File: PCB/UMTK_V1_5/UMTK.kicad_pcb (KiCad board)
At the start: 4 copper layers, 170 x 80 mm, 97 parts, among them J1 Motor Out, J2 ESTOP, J3 LOADCELL, J5 PJ-102BH, J8 10033526-N3212LF, Q1 Q_PNP_BEC, U1 DRV8873SPWPRQ1, U10 LM2576HVS-5, U11 SN74LVC1T45DCK, U12 SN74LVC1T45DCK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

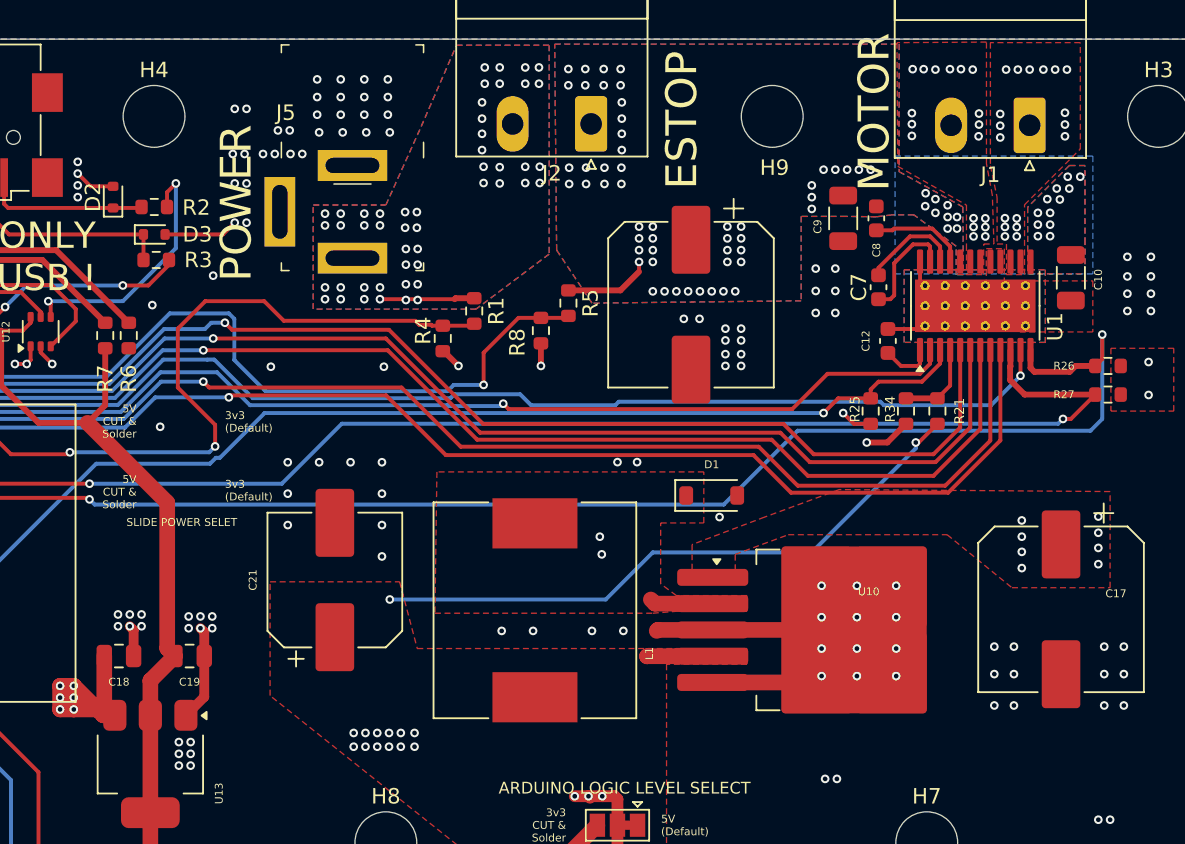
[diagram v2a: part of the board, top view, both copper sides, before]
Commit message: Add a bit of decoupling for 7seg driver
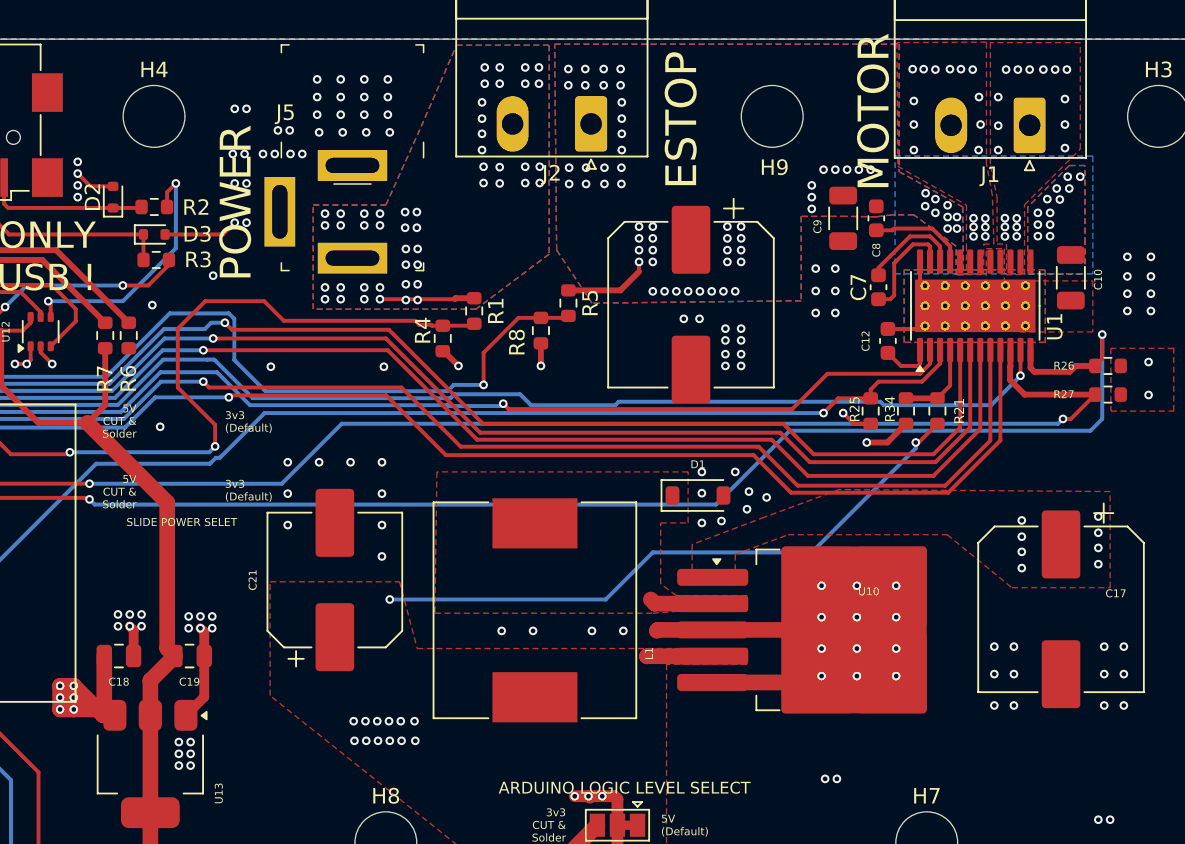
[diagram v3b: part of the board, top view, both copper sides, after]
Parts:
- moved D1 0.89 mm to (155.2, 49.5)
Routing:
- net GND: vias 269 -> 272
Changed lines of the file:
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@@
 	(footprint "Diode_SMD:D_SOD-123"
 		(layer "F.Cu")
-		(at 156.083 49.53)
+		(at 155.195 49.53)
 		(descr "SOD-123")
 		(tags "SOD-123")
@@
 	)
 	(via
+		(at 158.369 50.419)
+		(size 0.56)
+		(drill 0.3)
+		(layers "F.Cu" "B.Cu")
+		(free yes)
+		(net 4)
+	)
+	(via
 		(at 30.226 59.69)
 		(size 0.56)
@@
 	)
 	(via
-		(at 148.971 53.34)
-		(size 0.56)
-		(drill 0.3)
-		(layers "F.Cu" "B.Cu")
-		(free yes)
-		(net 4)
-	)
-	(via
 		(at 46.99 36.703)
 		(size 0.56)
@@
 	)
 	(via
+		(at 155.448 49.382)
+		(size 0.56)
+		(drill 0.3)
+		(layers "F.Cu" "B.Cu")
+		(free yes)
+		(net 4)
+	)
+	(via
 		(at 121.605 67.009)
 		(size 0.56)
@@
 	)
 	(via
-		(at 149.987 47.371)
+		(at 155.448 51.308)
+		(size 0.56)
+		(drill 0.3)
+		(layers "F.Cu" "B.Cu")
+		(free yes)
+		(net 4)
+	)
+	(via
+		(at 157.607 48.006)
 		(size 0.56)
 		(drill 0.3)
@@
 	)
 	(via
-		(at 156.591 50.927)
+		(at 156.718 51.181)
 		(size 0.56)
 		(drill 0.3)
@@
 	)
 	(via
+		(at 158.496 49.276)
+		(size 0.56)
+		(drill 0.3)
+		(layers "F.Cu" "B.Cu")
+		(free yes)
+		(net 4)
+	)
+	(via
 		(at 157.988 38.735)
 		(size 0.56)
@@
 	)
 	(via
-		(at 148.844 52.196998)
+		(at 115.062 29.464)
 		(size 0.56)
 		(drill 0.3)
@@
 	)
 	(via
-		(at 115.062 29.464)
+		(at 122.24 57.357)
 		(size 0.56)
 		(drill 0.3)
 		(layers "F.Cu" "B.Cu")
-		(free yes)
 		(net 4)
 	)
 	(via
-		(at 122.24 57.357)
+		(at 159.639 49.657)
 		(size 0.56)
 		(drill 0.3)
 		(layers "F.Cu" "B.Cu")
+		(free yes)
 		(net 4)
 	)
@@
 	)
 	(via
-		(at 151.257 47.371)
+		(at 155.448 48.006)
 		(size 0.56)
 		(drill 0.3)
@@
 	)
 	(via
-		(at 133.6802 64.897)
+		(at 133.6802 64.135)
 		(size 0.56)
 		(drill 0.3)
@@
 	)
 	(via
-		(at 134.4422 65.786)
+		(at 134.493 65.405)
 		(size 0.56)
 		(drill 0.3)
@@
 	)
 	(via
-		(at 135.9662 65.786)
+		(at 136.017 65.405)
 		(size 0.56)
 		(drill 0.3)
@@
 	)
 	(via
-		(at 134.4422 64.897)
+		(at 134.4422 64.135)
 		(size 0.56)
 		(drill 0.3)
@@
 	)
 	(via
-		(at 132.9182 64.897)
+		(at 132.9182 64.135)
 		(size 0.56)
 		(drill 0.3)
@@
 	)
 	(via
-		(at 132.9182 65.786)
+		(at 132.969 65.405)
 		(size 0.56)
 		(drill 0.3)
@@
 	)
 	(via
-		(at 135.2042 64.897)
+		(at 135.2042 64.135)
 		(size 0.56)
 		(drill 0.3)
@@
 	)
 	(via
-		(at 136.8552 64.897)
+		(at 136.8552 64.135)
 		(size 0.56)
 		(drill 0.3)
@@
 	)
 	(via
-		(at 135.2042 65.786)
+		(at 135.255 65.405)
 		(size 0.56)
 		(drill 0.3)
@@
 	)
 	(via
-		(at 133.6802 65.786)
+		(at 133.731 65.405)
 		(size 0.56)
 		(drill 0.3)
@@
 	)
 	(via
-		(at 136.8552 65.786)
+		(at 136.906 65.405)
 		(size 0.56)
 		(drill 0.3)
@@
 	)
 	(via
-		(at 135.9662 64.897)
+		(at 135.9662 64.135)
 		(size 0.56)
 		(drill 0.3)
@@
 	)
 	(segment
-		(start 161.644724 45.339)
-		(end 180.594 45.339)
+		(start 180.594 45.339)
+		(end 181.356 44.577)
 		(width 0.254)
 		(layer "B.Cu")
@@
 	)
 	(segment
-		(start 116.159 50.119)
-		(end 156.864724 50.119)
+		(start 156.356724 50.119)
+		(end 161.136724 45.339)
 		(width 0.254)
 		(layer "B.Cu")
@@
 	)
 	(segment
-		(start 115.824 49.784)
-		(end 116.159 50.119)
+		(start 161.136724 45.339)
+		(end 180.594 45.339)
 		(width 0.254)
 		(layer "B.Cu")
@@
 	)
 	(segment
-		(start 180.594 45.339)
-		(end 181.356 44.577)
+		(start 116.159 50.119)
+		(end 156.356724 50.119)
 		(width 0.254)
 		(layer "B.Cu")
@@
 	)
 	(segment
-		(start 156.864724 50.119)
-		(end 161.644724 45.339)
+		(start 115.824 49.784)
+		(end 116.159 50.119)
 		(width 0.254)
 		(layer "B.Cu")
@@
 	)
 	(via
-		(at 169.037 24.7904)
+		(at 169.164 24.003)
 		(size 0.56)
 		(drill 0.3)
@@
 	)
 	(via
-		(at 169.037 25.5016)
+		(at 169.164 25.527)
 		(size 0.56)
 		(drill 0.3)
@@
 	)
 	(via
-		(at 173.3804 25.527)
+		(at 173.482 25.527)
 		(size 0.56)
 		(drill 0.3)
@@
 	)
 	(via
-		(at 173.355 26.289)
+		(at 173.355 27.178)
 		(size 0.56)
 		(drill 0.3)
@@
 	)
 	(via
-		(at 173.3804 24.8158)
+		(at 173.3804 23.749)
 		(size 0.56)
 		(drill 0.3)
@@
 	)
 	(via
-		(at 169.037 26.2636)
+		(at 169.164 27.178)
 		(size 0.56)
 		(drill 0.3)
@@
 	)
 	(via
-		(at 174.752 26.3652)
+		(at 174.625 27.178)
 		(size 0.56)
 		(drill 0.3)
@@
 	)
 	(via
-		(at 178.943 24.765)
+		(at 178.943 23.876)
 		(size 0.56)
 		(drill 0.3)
@@
 	)
 	(via
-		(at 178.943 26.289)
+		(at 178.943 27.051)
 		(size 0.56)
 		(drill 0.3)
@@
 	)
 	(via
-		(at 174.752 24.8412)
+		(at 174.625 23.749)
 		(size 0.56)
 		(drill 0.3)
@@
 	)
 	(via
-		(at 174.752 25.6032)
+		(at 174.625 25.6032)
 		(size 0.56)
 		(drill 0.3)
@@
 			(pts
 				(xy 138.303 48.006) (xy 138.176 57.15) (xy 152.273 57.15) (xy 153.797 57.023) (xy 158.369 57.023)
-				(xy 158.369 56.007) (xy 153.797 56.007) (xy 152.781 55.245) (xy 152.781 51.308) (xy 155.575 51.308)
-				(xy 155.575 48.006)
+				(xy 158.369 56.007) (xy 153.797 56.007) (xy 152.781 55.245) (xy 152.781 51.308) (xy 154.559 51.308)
+				(xy 154.559 48.006)
 			)
 		)
@@
 		(hatch edge 0.5)
 		(priority 9)
-		(connect_pads yes
+		(connect_pads thru_hole_only
 			(clearance 0.1524)
 		)
@@
 		(fill yes
 			(thermal_gap 0.5)
-			(thermal_bridge_width 0.5)
+			(thermal_bridge_width 1.016)
 		)
 		(polygon
@@
 		(hatch edge 0.5)
 		(priority 3)
-		(connect_pads yes
+		(connect_pads thru_hole_only
 			(clearance 0.1524)
 		)
@@
 		(fill yes
 			(thermal_gap 0.5)
-			(thermal_bridge_width 0.5)
+			(thermal_bridge_width 1.016)
 		)
 		(polygon
@@
 		(filled_areas_thickness no)
 		(fill yes
-			(thermal_gap 0.5)
-			(thermal_bridge_width 0.5)
+			(thermal_gap 0.508)
+			(thermal_bridge_width 1.016)
 			(island_removal_mode 1)
-			(island_area_min 9.999999)
+			(island_area_min 9.999998)
 		)
 		(polygon
@@
 		(fill yes
 			(thermal_gap 0.5)
-			(thermal_bridge_width 0.5)
+			(thermal_bridge_width 1.016)
 			(island_removal_mode 1)
-			(island_area_min 9.999999)
+			(island_area_min 9.999998)
 		)
 		(polygon

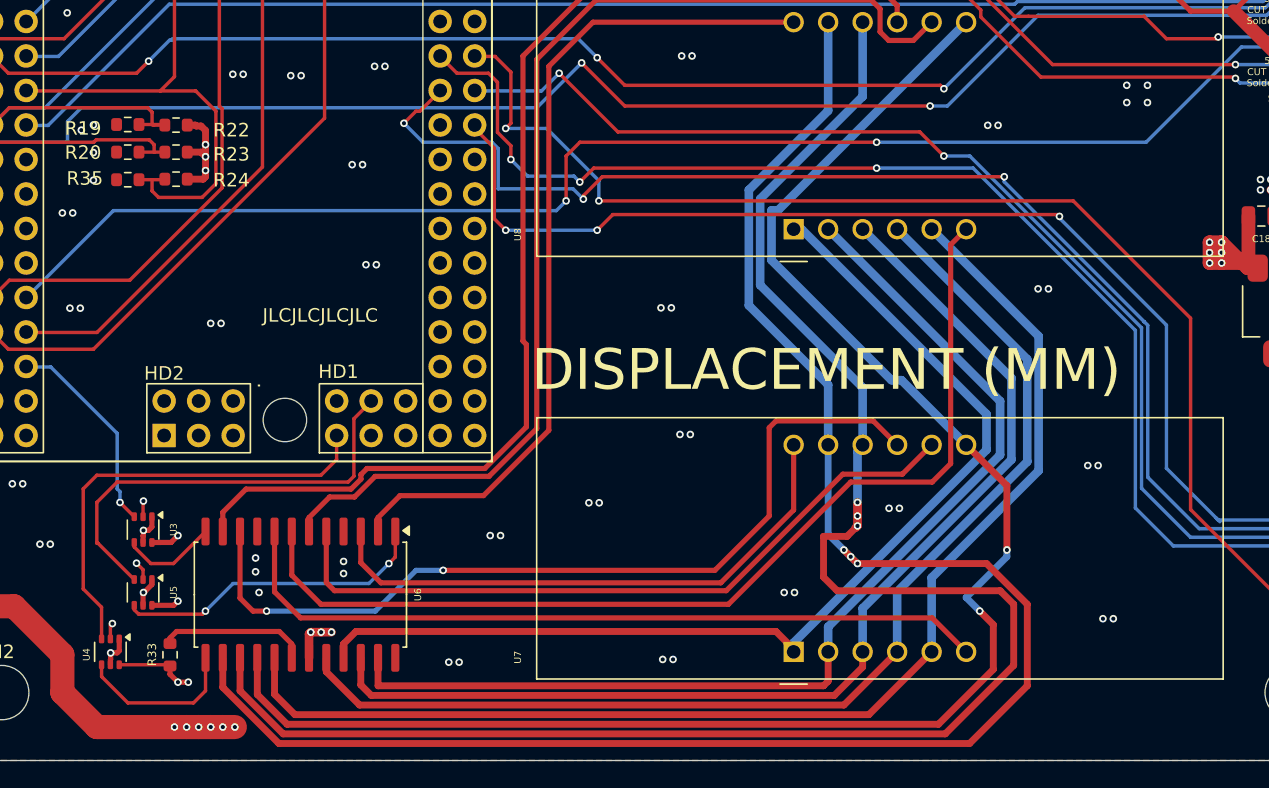
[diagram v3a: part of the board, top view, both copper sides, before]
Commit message: Add devoupling for 7seg
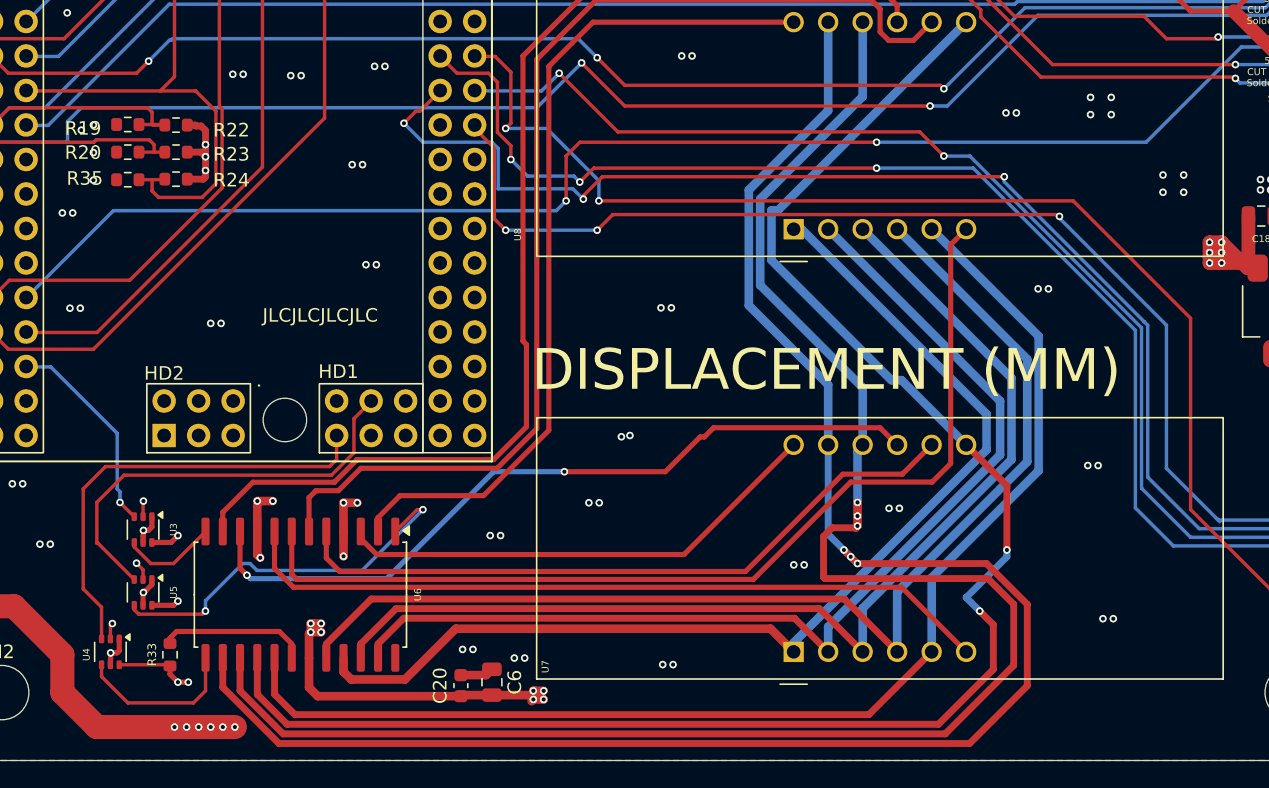
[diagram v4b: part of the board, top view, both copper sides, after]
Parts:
- added C20: 0.1u, Capacitor_SMD:C_0603_1608Metric, F.Cu at (58.8, 94.5)
- added C6: 10u, Capacitor_SMD:C_0805_2012Metric, F.Cu at (61.1, 94.2)
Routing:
- net +5V: track 262.1 -> 287.0 mm, vias 50 -> 55
- net GND: track 65.4 -> 78.2 mm, vias 272 -> 279
- net Net-(U6-DIG_5): track 64.0 -> 56.5 mm
- net Net-(U6-DIG_4): track 41.8 -> 36.2 mm
- net Net-(U5-B): track 23.3 -> 28.5 mm
- net Net-(U6-DIG_6): track 53.0 -> 50.8 mm
- net Net-(U6-SEG_E): track 78.3 -> 79.9 mm
- net Net-(U6-DIG_3): track 74.6 -> 73.1 mm
- net Net-(U6-SEG_D): track 79.1 -> 77.6 mm
- net Net-(U6-DIG_7): track 57.2 -> 56.2 mm
- net /7Seg_Display/DIN: track 32.6 -> 31.6 mm
- net Net-(U6-SEG_DP): track 81.4 -> 80.6 mm
- net Net-(U6-DIG_2): track 81.4 -> 82.2 mm

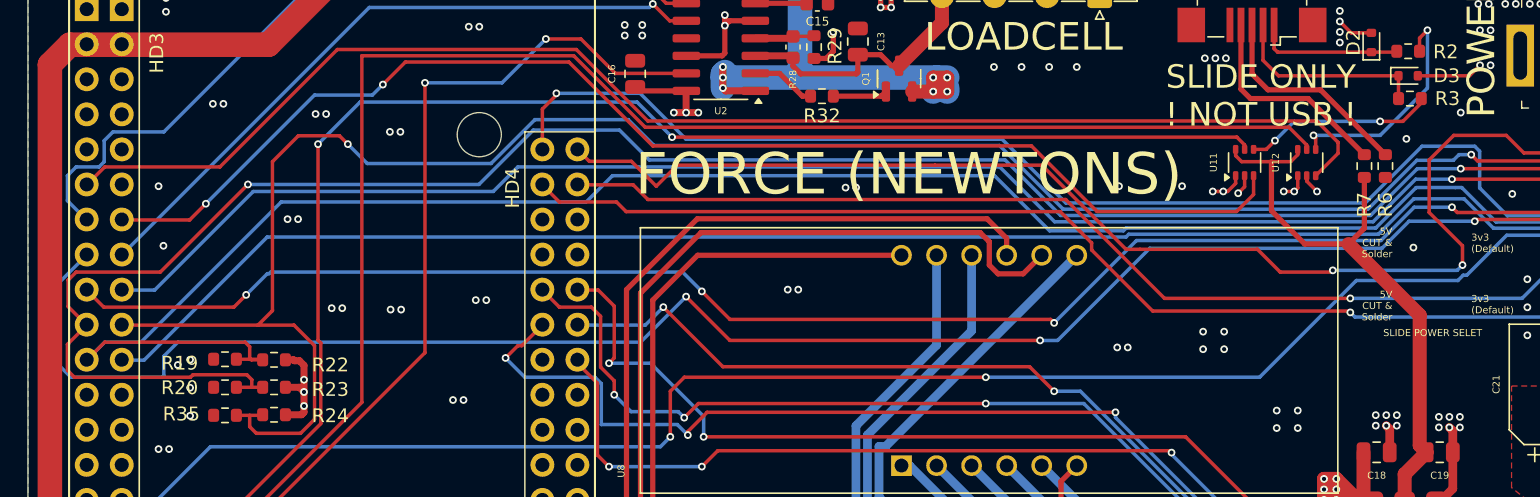
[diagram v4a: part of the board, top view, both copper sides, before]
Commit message: Move interrupr pin to 3, Move motor sleep to 14 so 13 can LED
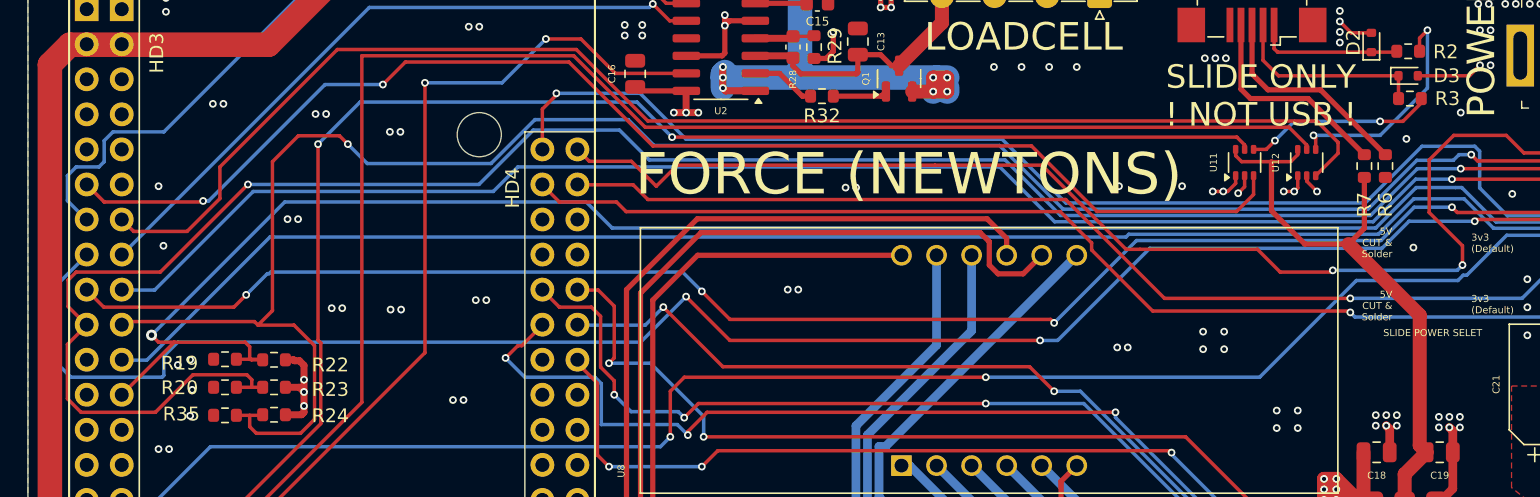
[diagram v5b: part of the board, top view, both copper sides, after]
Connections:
- A2 pad D13: /Arduino/MOT_nSLEEP -> unconnected-(A2-PadD13)
- A2 pad D14: unconnected-(A2-D14/TX3-PadD14) -> /Arduino/MOT_nSLEEP
- A2 pad D3: /Arduino/SLIDE_DAT -> /Arduino/SLIDE_CLK
- A2 pad D4: /Arduino/SLIDE_CLK -> /Arduino/SLIDE_DAT
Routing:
- net /Arduino/MOT_nSLEEP: track 180.6 -> 173.8 mm, vias 1 -> 2
- net /Arduino/MOT_nOL: track 191.5 -> 194.8 mm
- net /Arduino/SLIDE_CLK: track 93.1 -> 95.6 mm
- net /Arduino/SLIDE_DAT: track 100.6 -> 101.2 mm
